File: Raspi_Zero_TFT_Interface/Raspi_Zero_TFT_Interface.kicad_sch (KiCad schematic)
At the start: 15 parts, among them CN1 USB_C_Receptacle_PowerOnly_6P, CN2 B2B-XH-A, CN3 Molex FPC 541044031, CN4 Molex FPC 52271-0679, CN5 Conn_02x20_Odd_Even, J1 522070860, U1 AP5725WG-7

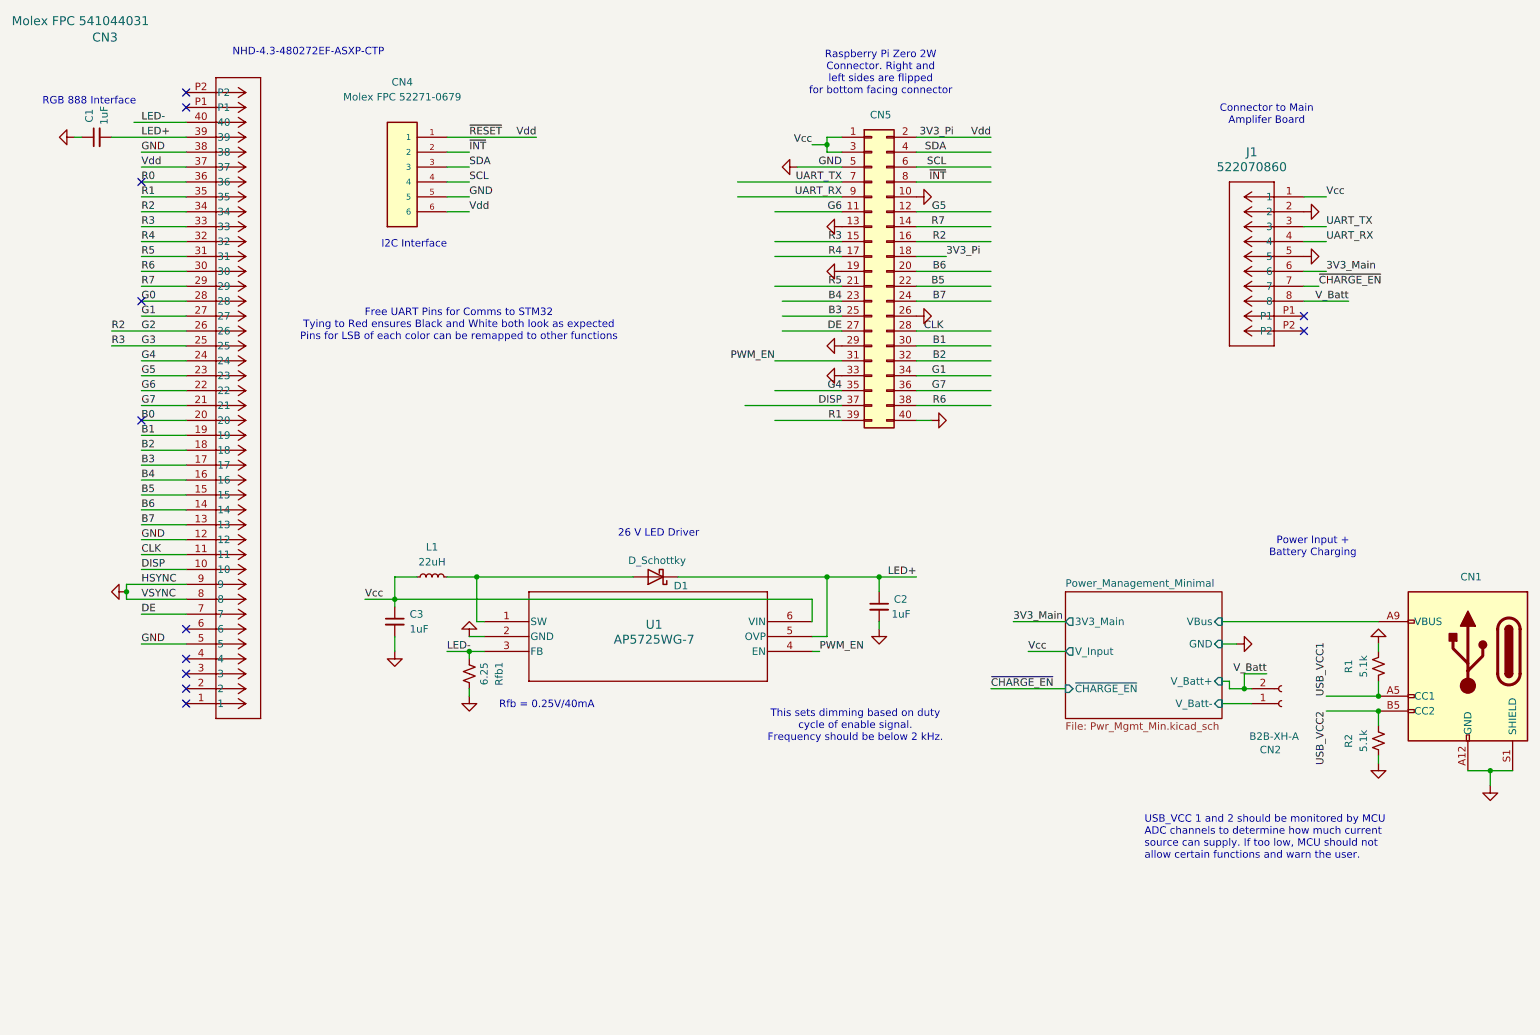
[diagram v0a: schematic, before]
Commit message: First Pass Schematic Fixes for Power Management Board
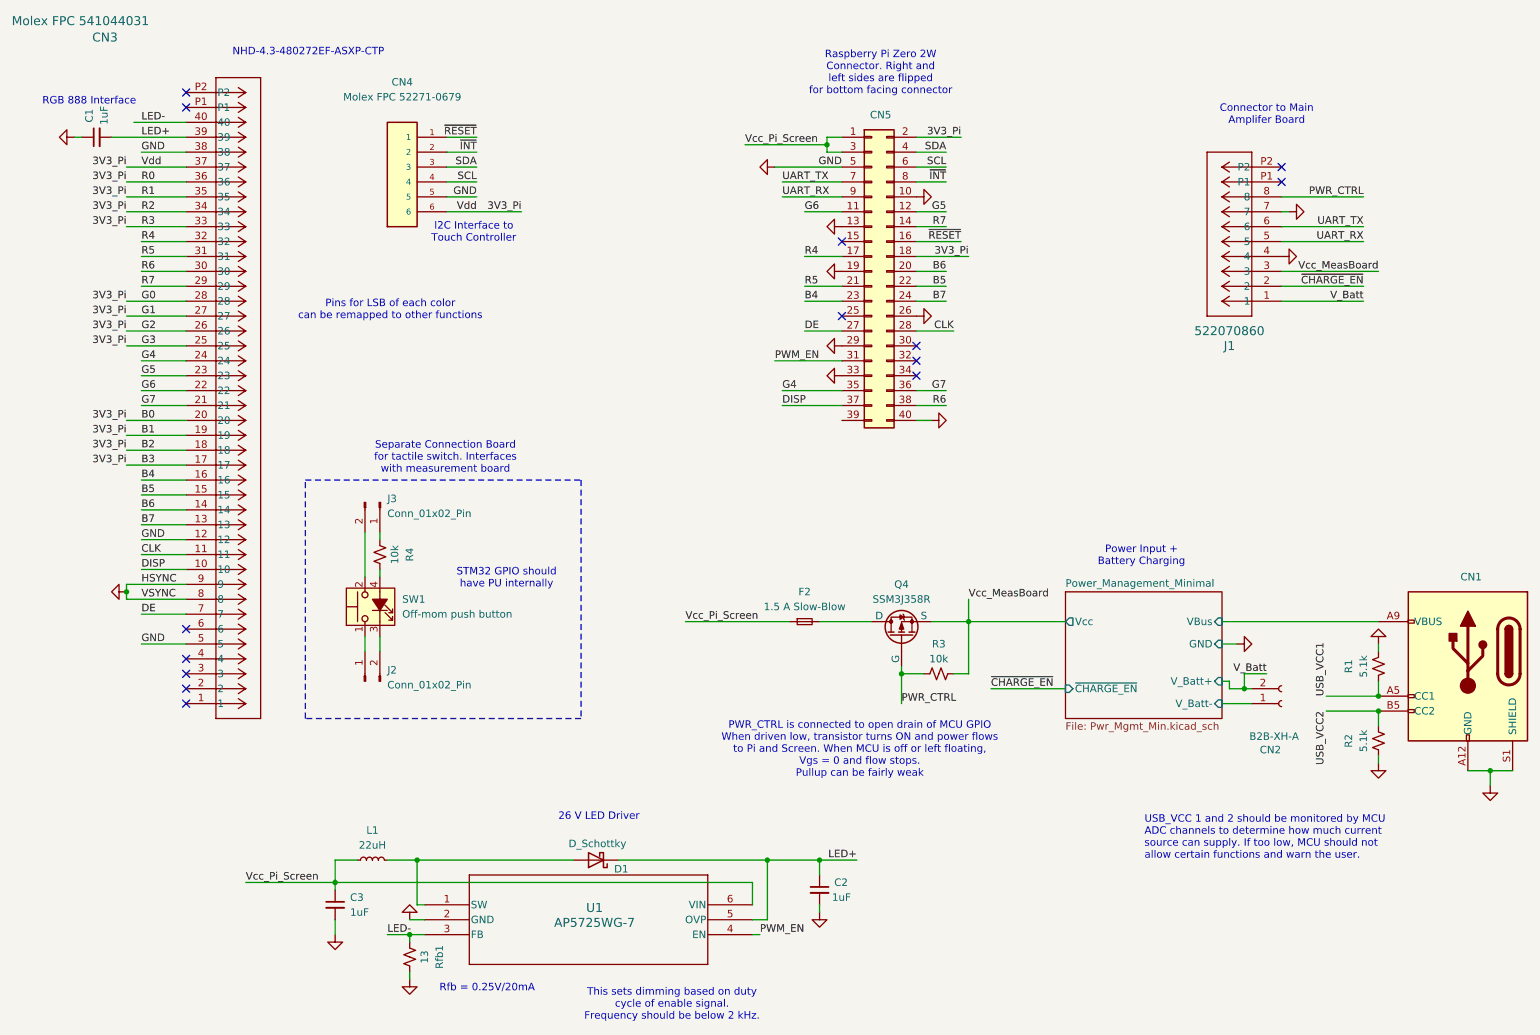
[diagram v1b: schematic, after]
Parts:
- added F2: 1.5 A Slow-Blow, symbol Device:Fuse_Small
- added J2, J3: Conn_01x02_Pin, symbol Connector:Conn_01x02_Pin
- added Q4: SSM3J358R, Package_TO_SOT_SMD:SOT-23-3, symbol FrontEndPrototype_Rev1-rescue:SSM3J358R
- added R3, R4: 10k, Resistor_SMD:R_0603_1608Metric_Pad0.98x0.95mm_HandSolder, symbol Device:R_Small_US
- added SW1: Off-mom push button, symbol Switch:SW_Push_LED
- Rfb1: value 6.25 -> 13
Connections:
- net 3V3_Main is gone; now on net UART_TX: J1.6
- net B0 is gone; now on net 3V3_Pi: CN3.20
- net G0 is gone; now on net 3V3_Pi: CN3.28
- net R0 is gone; now on net 3V3_Pi: CN3.36
- net 3V3_Pi: now also CN3.17, CN3.18, CN3.19, CN3.25, CN3.26, CN3.27, CN3.33, CN3.34, CN3.35; no longer CN4.1
- net GND: now also J1.4, J1.7; no longer J1.2, J1.5
- net UART_RX: now also J1.5; no longer J1.4
- net UART_TX: no longer J1.3
- net V_Batt: now also J1.1; no longer J1.8
- net ~{CHARGE_EN}: now also J1.2; no longer J1.7
- net B1: no longer names the net of CN5.30 (Pin_30)
- net B1: no longer CN3.19
- net B2: no longer names the net of CN5.32 (Pin_32)
- net B2: no longer CN3.18
- net B3: no longer names the net of CN5.25 (Pin_25)
- net B3: no longer CN3.17
- net G1: no longer names the net of CN5.34 (Pin_34)
- net G1: no longer CN3.27
- removed net G2: CN3.26, CN3.34, CN5.16 (Pin_16)
- removed net G3: CN3.25, CN3.33, CN5.15 (Pin_15)
- net R1: no longer names the net of CN5.39 (Pin_39)
- net R1: no longer CN3.35
- net Vcc renamed Vcc_Pi_Screen
- net Vcc_Pi_Screen: now also F2.1; no longer J1.1
- new net: F2.2, Q4.3 (D)
- new net: J3.1 (Pin_1), R4.1
- new net: R4.2, SW1.4 (A)
- new net: J2.1 (Pin_1), SW1.1
- new net: J2.2 (Pin_2), SW1.3 (K)
- new net: J3.2 (Pin_2), SW1.2
- new net PWR_CTRL: J1.8, Q4.1 (G), R3.1
- new net Vcc_MeasBoard: J1.3, Q4.2 (S), R3.2
- new net ~{RESET}: CN4.1, CN5.16 (Pin_16)
- no-connect marks 12 -> 14
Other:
- sheet Power_Management_Minimal ports: added Vcc; removed 3V3_Main, V_Input
- note added: "I2C Interface to Touch Controller"
- note added: "PWR_CTRL is connected to open drain of MCU GPIO When driven low, transistor turns ON and power flows to Pi and Screen. When MCU is off or left floating, Vgs = 0 and flow stops. Pullup can be fairly weak"
- note added: "Pins for LSB of each color can be remapped to other functions"
- note added: "Rfb = 0.25V/20mA"
- note added: "STM32 GPIO should have PU internally"
- note added: "Separate Connection Board for tactile switch. Interfaces with measurement board"
- note removed: "Free UART Pins for Comms to STM32 Tying to Red ensures Black and White both look as expected Pins for LSB of each color can be remapped to other functions"
- note removed: "I2C Interface"
- note removed: "Rfb = 0.25V/40mA"
- moved on the sheet: C2, C3, D1, J1, L1, Rfb1, U1

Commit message: Finished Rasp Board PCB Routing
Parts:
- removed J2, J3: Conn_01x02_Pin, symbol Connector:Conn_01x02_Pin
- added J2: Conn_01x04_Pin, Connector_PinHeader_2.54mm:PinHeader_1x04_P2.54mm_Vertical, symbol Connector:Conn_01x04_Pin
- added R5: 33, Resistor_SMD:R_0603_1608Metric_Pad0.98x0.95mm_HandSolder, symbol Device:R_Small_US
- F2: footprint (none) -> Fuse:Fuse_0603_1608Metric
- R4: value 10k -> 33
- SW1: footprint (none) -> GenII:TL1240_LED_Switch
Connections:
- net PWM_EN: now also R4.1; no longer CN5.31 (Pin_31)
- net UART_TX: now also R5.1; no longer CN5.7 (Pin_7)
- net at SW1.4 (A): now also J2.2 (Pin_2); no longer R4.2
- net at SW1.1: now also J2.4 (Pin_4)
- net at SW1.3 (K): now also J2.3 (Pin_3)
- net at SW1.2: now also J2.1 (Pin_1)
- net PWR_CTRL renamed ~{PWR_EN}
- new net: CN5.7 (Pin_7), R5.2
- new net: CN5.31 (Pin_31), R4.2
- no-connect marks 14 -> 15

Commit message: Final Rev3 Commit Post Submission
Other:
- moved on the sheet: F2
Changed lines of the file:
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@@
 	(wire
 		(pts
-			(xy 176.53 114.3) (xy 176.53 118.11)
+			(xy 176.53 116.84) (xy 176.53 118.11)
 		)
 		(stroke
@@
 	(wire
 		(pts
-			(xy 151.13 118.11) (xy 160.02 118.11)
+			(xy 153.67 118.11) (xy 160.02 118.11)
 		)
 		(stroke
@@
 	(wire
 		(pts
-			(xy 128.27 118.11) (xy 146.05 118.11)
+			(xy 129.54 118.11) (xy 148.59 118.11)
 		)
 		(stroke
@@
 	)
 	(label "Vcc_MeasBoard"
-		(at 176.53 114.3 0)
+		(at 176.53 116.84 0)
 		(fields_autoplaced yes)
 		(effects
@@
 	)
 	(label "Vcc_Pi_Screen"
-		(at 128.27 118.11 0)
+		(at 129.54 118.11 0)
 		(fields_autoplaced yes)
 		(effects
@@
 	(symbol
 		(lib_id "Device:Fuse_Small")
-		(at 148.59 118.11 0)
+		(at 151.13 118.11 0)
 		(unit 1)
 		(exclude_from_sim no)
@@
 		(dnp no)
 		(property "Reference" "F2"
-			(at 148.59 113.03 0)
+			(at 151.13 113.03 0)
 			(effects
 				(font
@@
 		)
 		(property "Value" "1.5 A Slow-Blow"
-			(at 148.59 115.57 0)
+			(at 151.13 115.57 0)
 			(effects
 				(font
@@
 		)
 		(property "Footprint" "Fuse:Fuse_0603_1608Metric"
-			(at 148.59 118.11 0)
+			(at 151.13 118.11 0)
 			(effects
 				(font
@@
 		)
 		(property "Datasheet" "~"
-			(at 148.59 118.11 0)
+			(at 151.13 118.11 0)
 			(effects
 				(font
@@
 		)
 		(property "Description" "Fuse, small symbol"
-			(at 148.59 118.11 0)
+			(at 151.13 118.11 0)
 			(effects
 				(font
